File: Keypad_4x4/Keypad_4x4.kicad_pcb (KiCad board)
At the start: 2 copper layers, 51 x 41.5 mm, 17 parts, among them J1 Conn_01x08

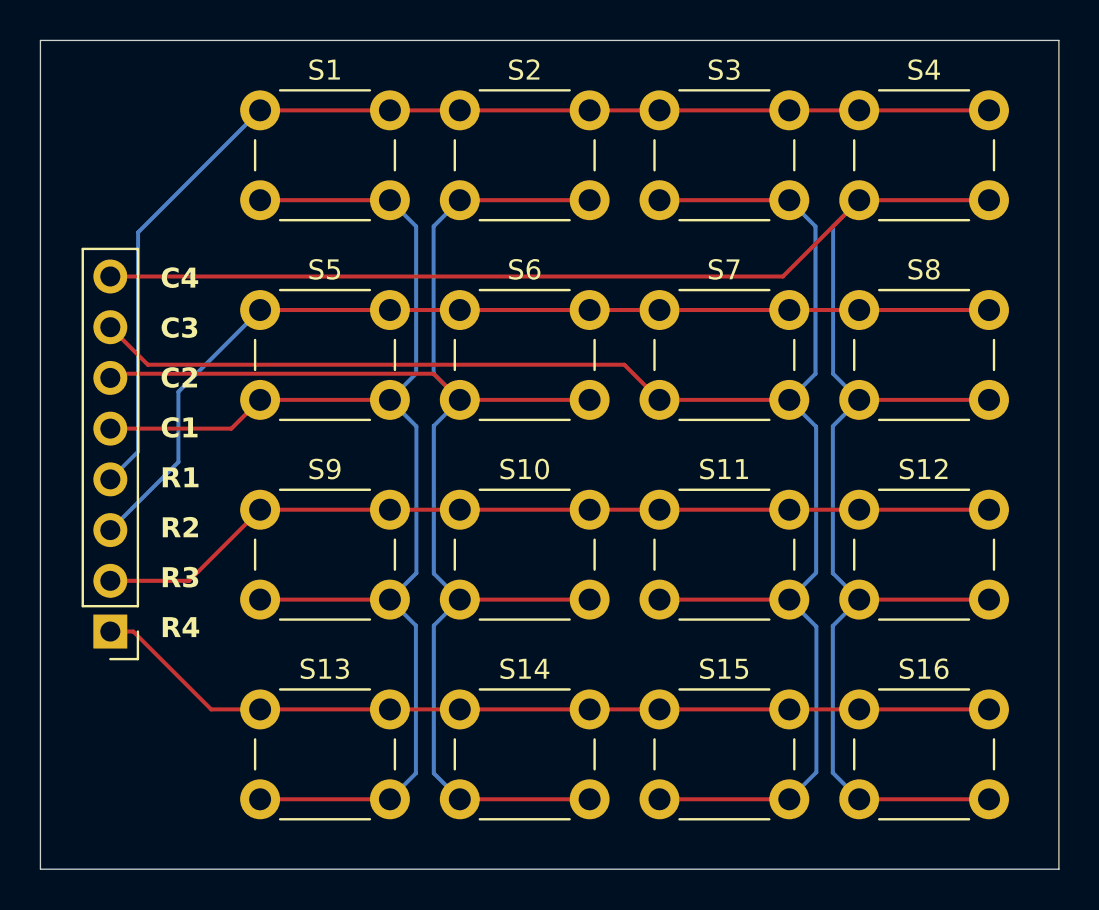
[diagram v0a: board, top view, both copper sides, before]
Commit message: Modified Keypad 4x4
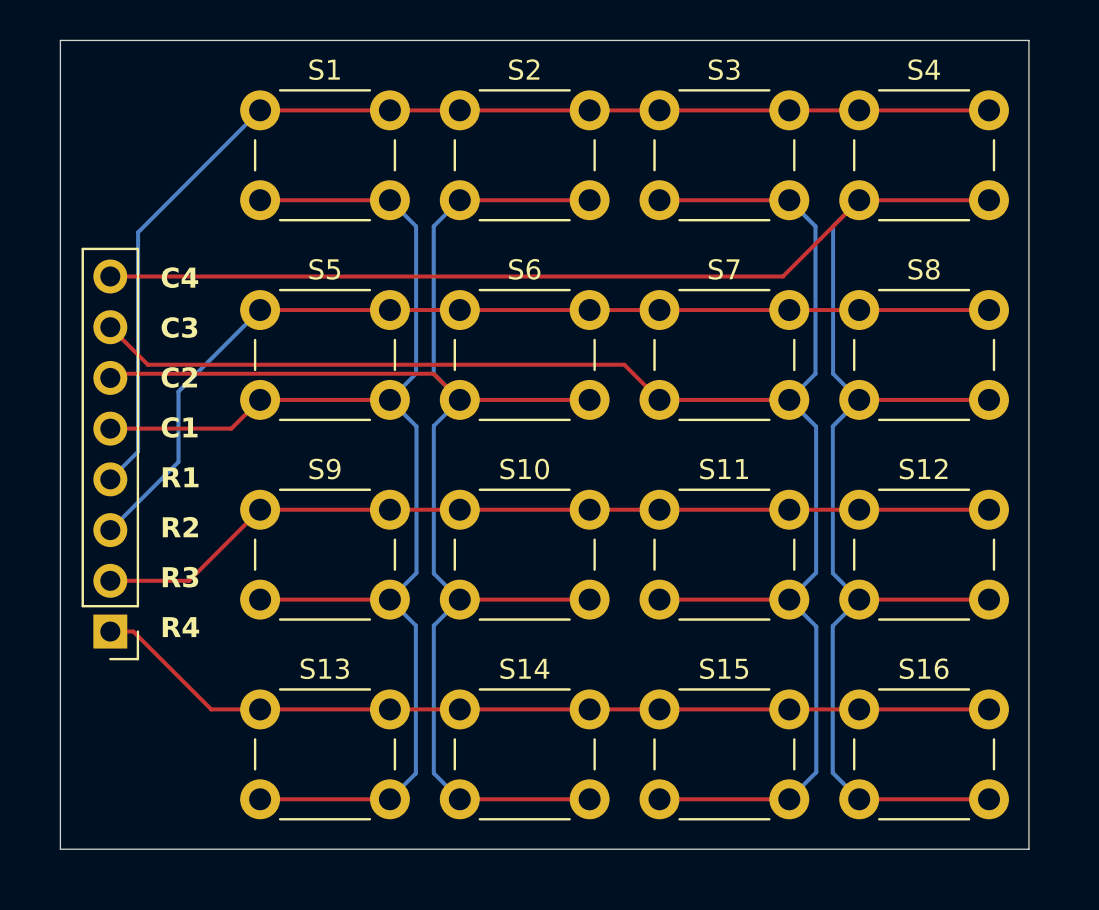
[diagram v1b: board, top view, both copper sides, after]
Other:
- board size 51 x 41.5 mm -> 48.5 x 40.5 mm
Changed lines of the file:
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@@
 	)
 	(gr_rect
-		(start 89 96.5)
-		(end 140 138)
+		(start 90 96.5)
+		(end 138.5 137)
 		(stroke
 			(width 0.05)
